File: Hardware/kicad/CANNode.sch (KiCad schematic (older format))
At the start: 49 parts, among them J1 Conn_01x04, J11 Conn_01x04, J12 Conn_01x04, J2 Conn_01x04, J21 Conn_01x04, J31 Conn_01x04, J41 Conn_01x04, J42 Conn_01x04, J43 Conn_01x04, J44 Conn_01x04, J61 Conn_02x04_Odd_Even, J81 Conn_01x10, J91 Conn_01x04, U1 Teensy3.2, U2 SN65HVD230, U21 PCA9306, U31 MAX3485, U41 MAX3032, U91 LM1117-5.0

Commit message: new images (pdf)
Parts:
- MOD1: symbol 000_my_lib:DSN-MINI-360 -> CANNode-rescue:DSN-MINI-360-000_my_lib
- U1: symbol teensy:Teensy3.2 -> CANNode-rescue:Teensy3.2-teensy
- U41: symbol 000_my_lib:MAX3032 -> CANNode-rescue:MAX3032-000_my_lib
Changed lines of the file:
@@
 EESchema Schematic File Version 4
 LIBS:CANNode-cache
-EELAYER 26 0
+EELAYER 30 0
 EELAYER END
 $Descr User 9843 7874
@@
 $EndDescr
 $Comp
-L teensy:Teensy3.2 U1
+L CANNode-rescue:Teensy3.2-teensy U1
 U 1 1 5BE599D2
 P 7050 2600
@@
 $EndComp
 $Comp
-L 000_my_lib:DSN-MINI-360 MOD1
+L CANNode-rescue:DSN-MINI-360-000_my_lib MOD1
 U 1 1 5BE5A42C
 P 2450 5450
@@
 	5700 3300 5700 3850
 $Comp
-L 000_my_lib:MAX3032 U41
+L CANNode-rescue:MAX3032-000_my_lib U41
 U 1 1 5C608233
 P 2600 3350

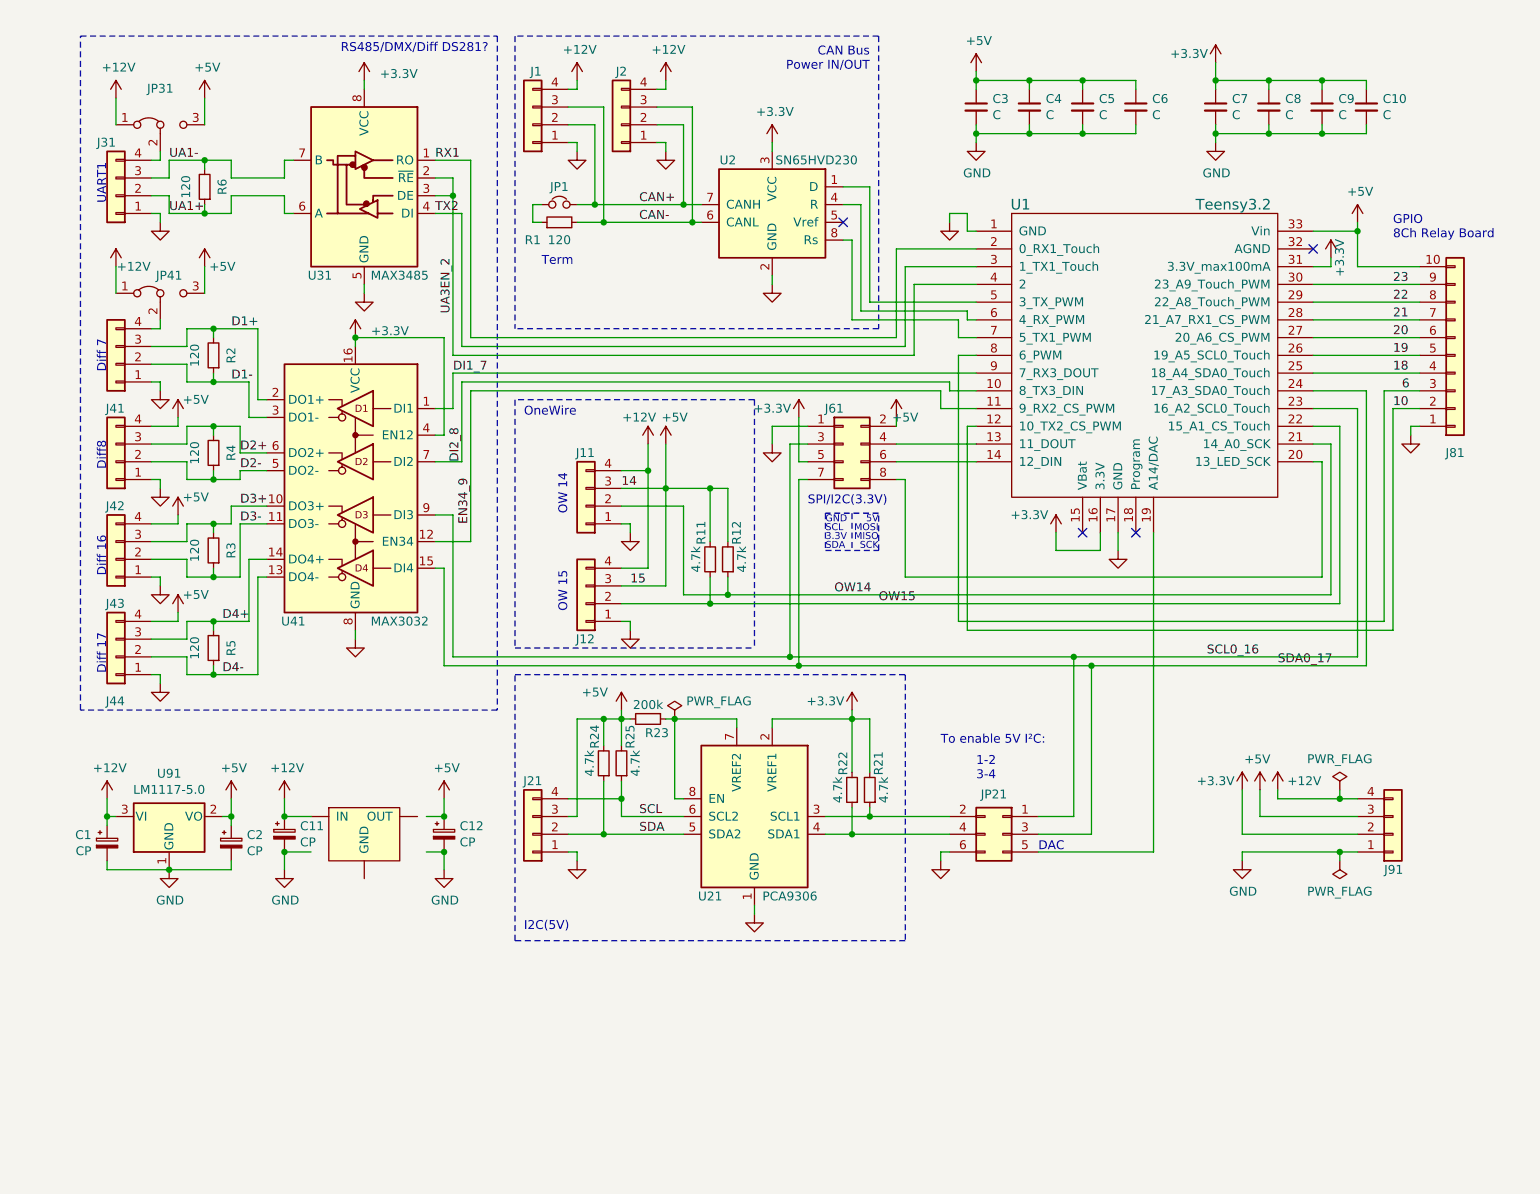
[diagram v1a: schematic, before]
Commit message: double RS485
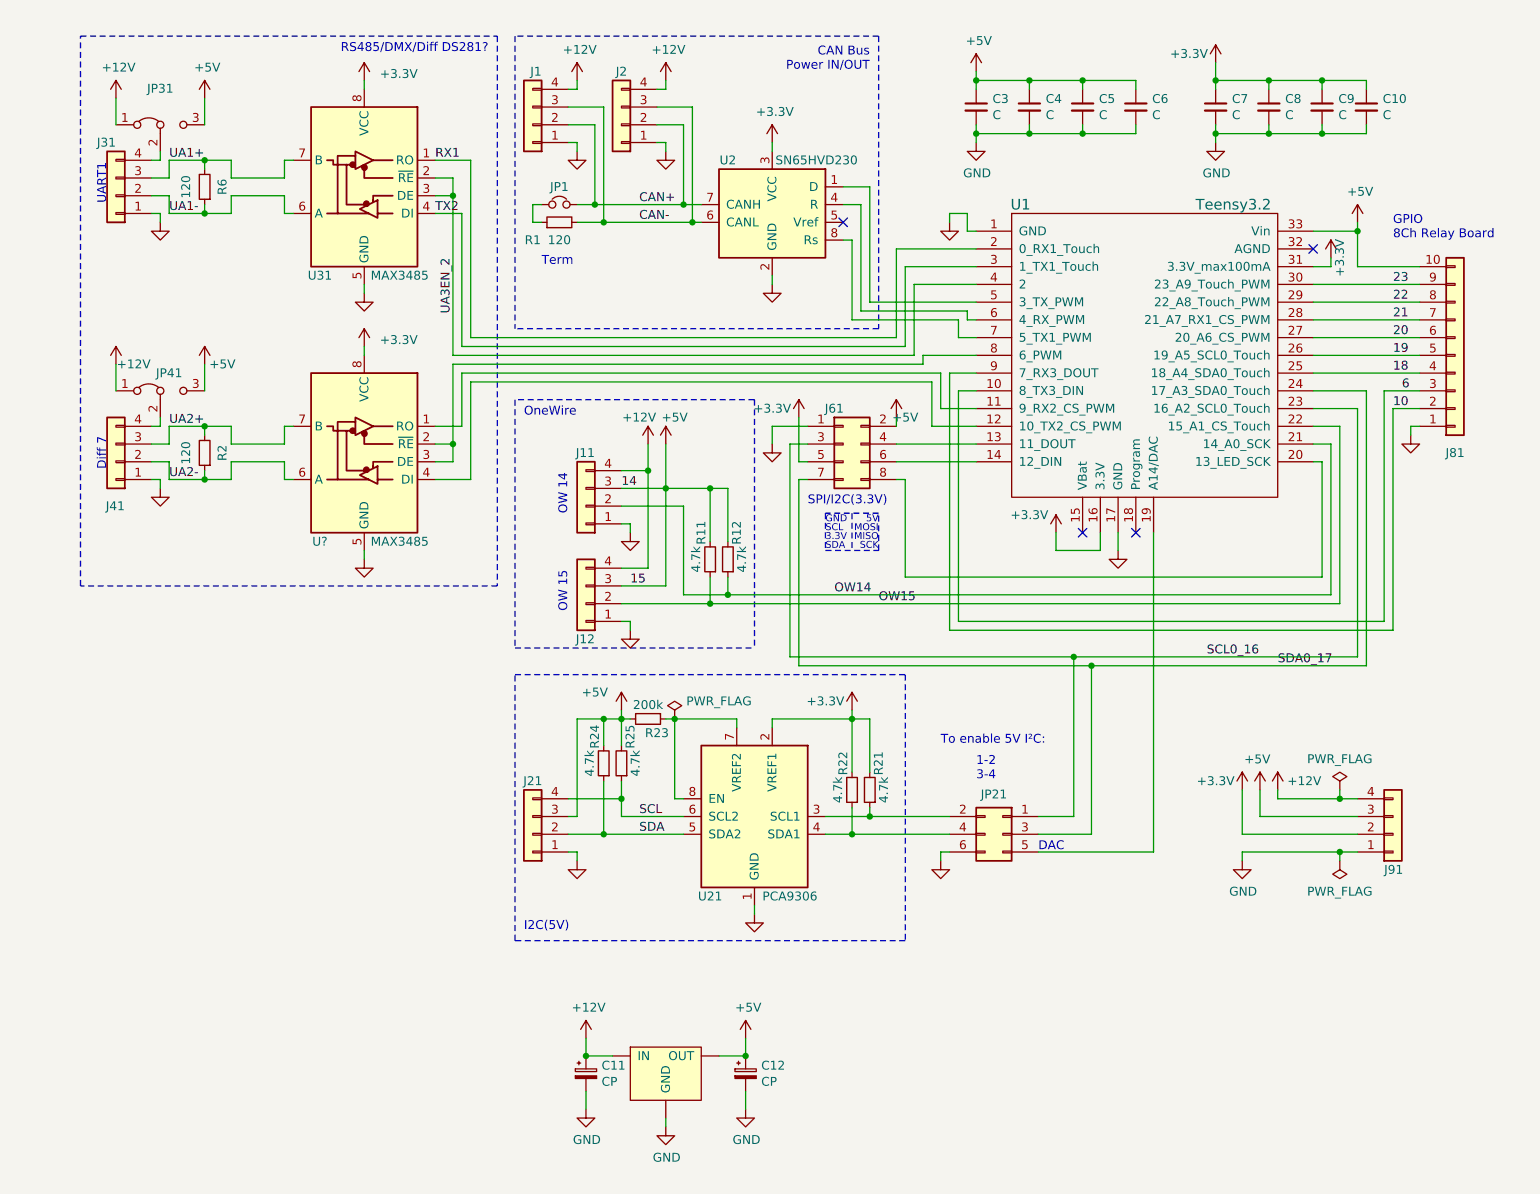
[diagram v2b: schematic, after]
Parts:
- removed C1, C2: CP, Capacitor_SMD:CP_Elec_3x5.4, symbol Device:CP_Small
- removed J42, J43, J44: Conn_01x04, Connector_PinHeader_2.54mm:PinHeader_1x04_P2.54mm_Vertical, symbol Connector_Generic:Conn_01x04
- removed R3, R4, R5: 120, Resistor_SMD:R_0805_2012Metric_Pad1.15x1.40mm_HandSolder, symbol Device:R_Small
- removed U41: MAX3032, Package_SO:SOIC-16_3.9x9.9mm_P1.27mm, symbol CANNode-rescue:MAX3032-000_my_lib
- removed U91: LM1117-5.0, Package_TO_SOT_SMD:SOT-223-3_TabPin2, symbol Regulator_Linear:LM1117-5.0
- added U?: MAX3485, Package_SO:SOIC-8_3.9x4.9mm_P1.27mm, symbol Interface_UART:MAX3485
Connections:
- net DI1_7 is gone; now on net 10: U1.9 (7_RX3_DOUT)
- net DI2_8 is gone; now on net 6: U1.10 (8_TX3_DIN)
- net +3V3: now also U?.8 (VCC)
- net +5V: now also MOD1.OUT
- net 10: no longer U1.12 (10_TX2_CS_PWM)
- net 6: no longer U1.8 (6_PWM)
- net GND: now also MOD1.GND, U?.5 (GND)
- net UA1+: now also J31.3 (Pin_3), R6.2, U31.7 (B); no longer J31.2 (Pin_2), R6.1, U31.6 (A)
- net UA1-: now also J31.2 (Pin_2), R6.1, U31.6 (A); no longer J31.3 (Pin_3), R6.2, U31.7 (B)
- net D1+ renamed UA2+
- net UA2+: now also U?.7 (B)
- net D1- renamed UA2-
- net UA2-: now also U?.6 (A)
- net EN34_9: no longer names the net of U1.11 (9_RX2_CS_PWM)
- net EN34_9: now also U?.1 (RO)
- new net: U1.12 (10_TX2_CS_PWM), U?.4 (DI)
- new net: U1.8 (6_PWM), U?.2 (~RE), U?.3 (DE)
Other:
- note removed: "Diff 16"
- note removed: "Diff 17"
- note removed: "Diff8"
- moved on the sheet: C11, C12, J41, JP41, R2

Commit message: second RS485 swapped with OW
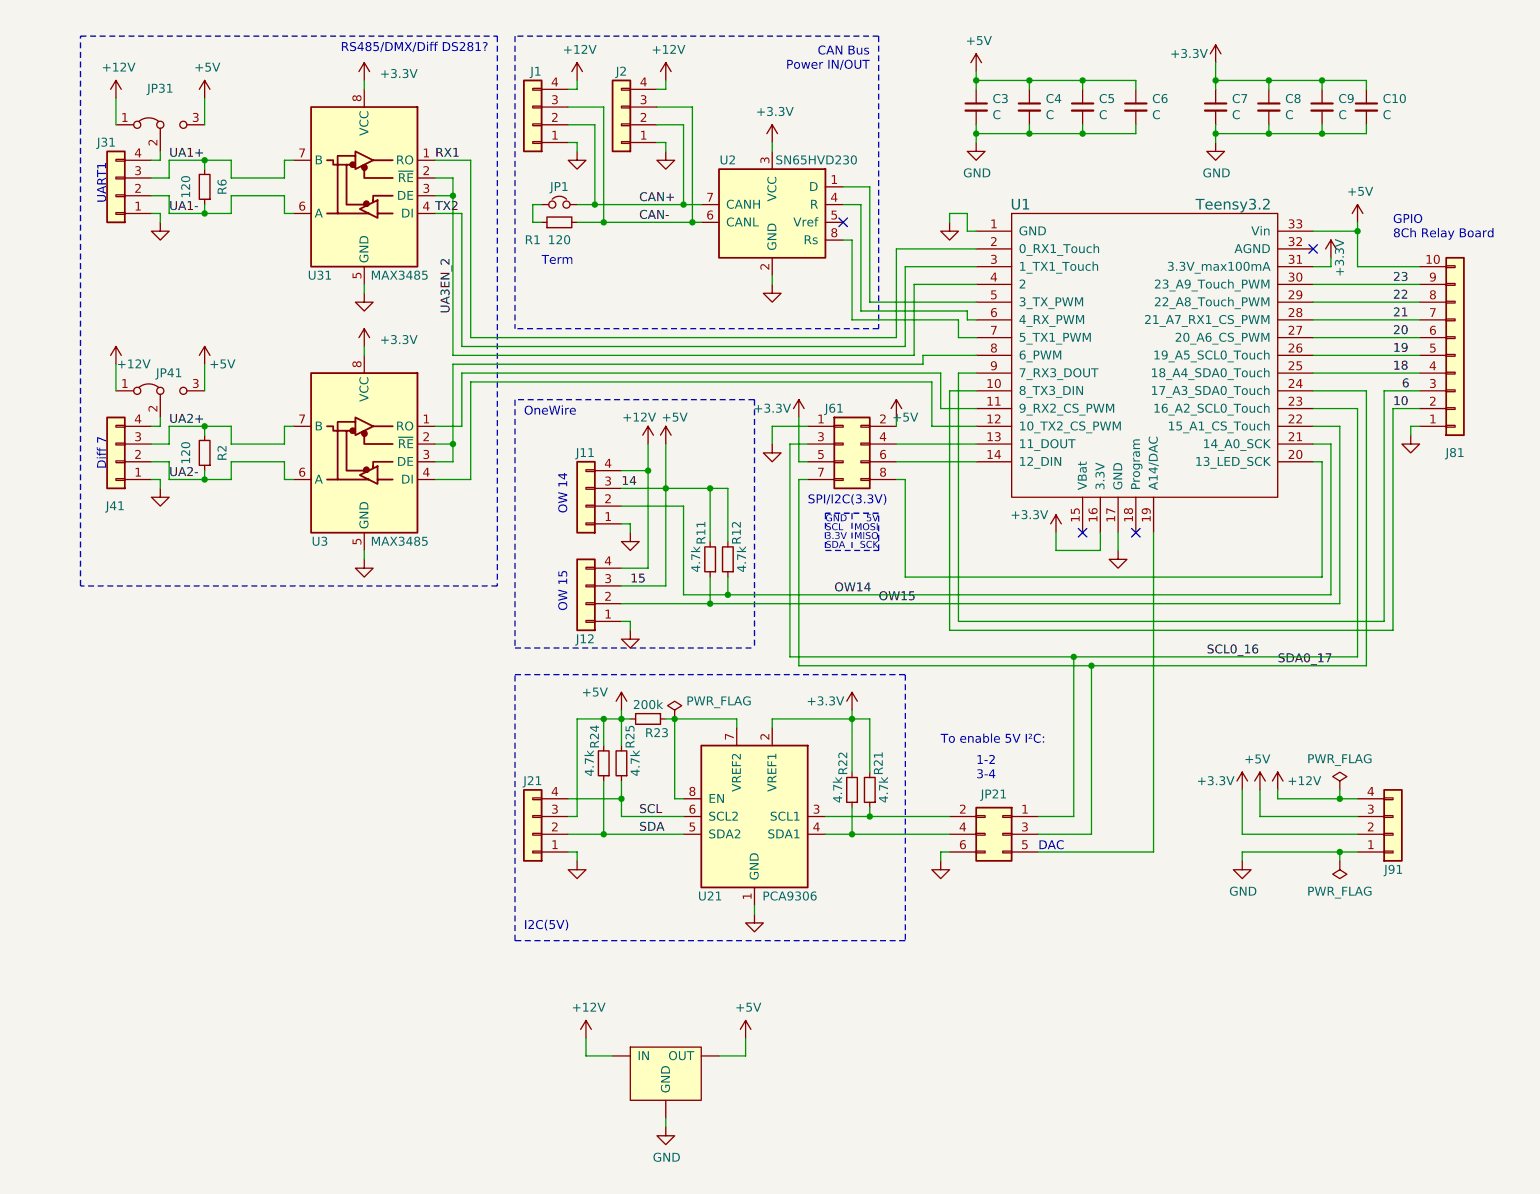
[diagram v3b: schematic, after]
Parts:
- removed C11, C12: CP, Capacitor_SMD:CP_Elec_3x5.4, symbol Device:CP_Small
- gave numbers to parts that had none: 1
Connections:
- net 10: now also U1.10 (8_TX3_DIN); no longer U1.9 (7_RX3_DOUT)
- net 6: now also U1.9 (7_RX3_DOUT); no longer U1.10 (8_TX3_DIN)

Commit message: pproaching v2.5
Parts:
- removed C5: C, Capacitor_SMD:C_0805_2012Metric_Pad1.15x1.40mm_HandSolder, symbol Device:C_Small
- removed J2, J91: Conn_01x04, CANNode:OWN_KF141V-P4_simple, symbol Connector_Generic:Conn_01x04
- added C1, C10, C11, C4: C, Capacitor_SMD:C_0805_2012Metric_Pad1.15x1.40mm_HandSolder, symbol Device:C_Small
- added H1, H2, H3, H4: MountingHole, MountingHole:MountingHole_3.5mm, symbol Mechanical:MountingHole
- added J8: Conn_01x03, 00_mylib:WAGO_243_3-Pole, symbol Connector_Generic:Conn_01x03
- added Log1, Log3: Logo, 00_mylib:LOGO_MID, symbol 00_mylib:Logo
- added Log2, Log4: Logo, Symbol:OSHW-Logo_5.7x6mm_Copper, symbol 00_mylib:Logo
- J1: footprint CANNode:OWN_KF141V-P4_simple -> 00_mylib:WAGO_243_4-Pole
- J2: renamed from J31; footprint CANNode:OWN_KF141V-P4_simple -> 00_mylib:OWN_KF141V-P4_simple
- J5: renamed from J41; footprint CANNode:OWN_KF141V-P4_simple -> 00_mylib:OWN_KF141V-P4_simple
- J6: renamed from J11; footprint CANNode:OWN_KF141V-P4_simple -> 00_mylib:WAGO_243_4-Pole
- MOD1: footprint CANNode:OWN_DC-DC -> 00_mylib:OWN_DC-DC; symbol CANNode-rescue:DSN-MINI-360-000_my_lib -> 00_mylib:OWN_DCDC-CANNode
- renumbered C3 to C2, C4 to C3, C6 to C5, C7 to C6, C8 to C7, C9 to C8, C10 to C9, J81 to J3, J61 to J4, J12 to J7, J21 to J9, JP31 to JP1, JP1 to JP2, JP41 to JP3, JP21 to JP4, R6 to R1, R21 to R10, R1 to R2, R2 to R3, R11 to R4, R12 to R5, R23 to R6, R24 to R7, R25 to R8, R22 to R9, U31 to U1, U1 to U3, U3 to U4, U21 to U5
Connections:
- net +12V: now also MOD1.IN+, C11.1, C4.1, J8.1 (Pin_1); no longer MOD1.IN
- net +5V: now also MOD1.OUT+, J8.2 (Pin_2); no longer MOD1.OUT
- net GND: now also JP4.1 (Pin_1), MOD1.IN-, MOD1.OUT-, C1.1, C10.1, C11.2, C4.2, J8.3 (Pin_3); no longer JP4.6 (Pin_6), MOD1.GND
- net SCL0_16: now also JP4.6 (Pin_6); no longer JP4.1 (Pin_1)
- net SDA0_17: now also JP4.4 (Pin_4); no longer JP4.3 (Pin_3)
- net TX2: now also U3.12 (10_TX2_CS_PWM), U4.4 (DI); no longer U1.4 (DI), U3.3 (1_TX1_Touch)
- net RX2: now reaches U3.11 (9_RX2_CS_PWM), U4.1 (RO)
- net at U3.19 (A14/DAC): now also JP4.2 (Pin_2); no longer JP4.5 (Pin_5)
- net at R10.1, U5.3 (SCL1): now also JP4.5 (Pin_5); no longer JP4.2 (Pin_2)
- net at R9.1, U5.4 (SDA1): now also JP4.3 (Pin_3); no longer JP4.4 (Pin_4)
- net at J2.4 (Pin_4), JP1.2 (C): now also C1.2
- net at J5.4 (Pin_4), JP3.2 (C): now also C10.2
- new net TX1: U1.4 (DI), U3.3 (1_TX1_Touch)
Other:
- moved on the sheet: C2, C3, C5, C6, C7, C8, C9, J1, JP1, JP2, JP3, R2
